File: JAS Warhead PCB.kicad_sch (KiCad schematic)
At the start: 8 parts, among them J7 Conn_01x02_Socket, U4 LD1117S50TR_SOT223

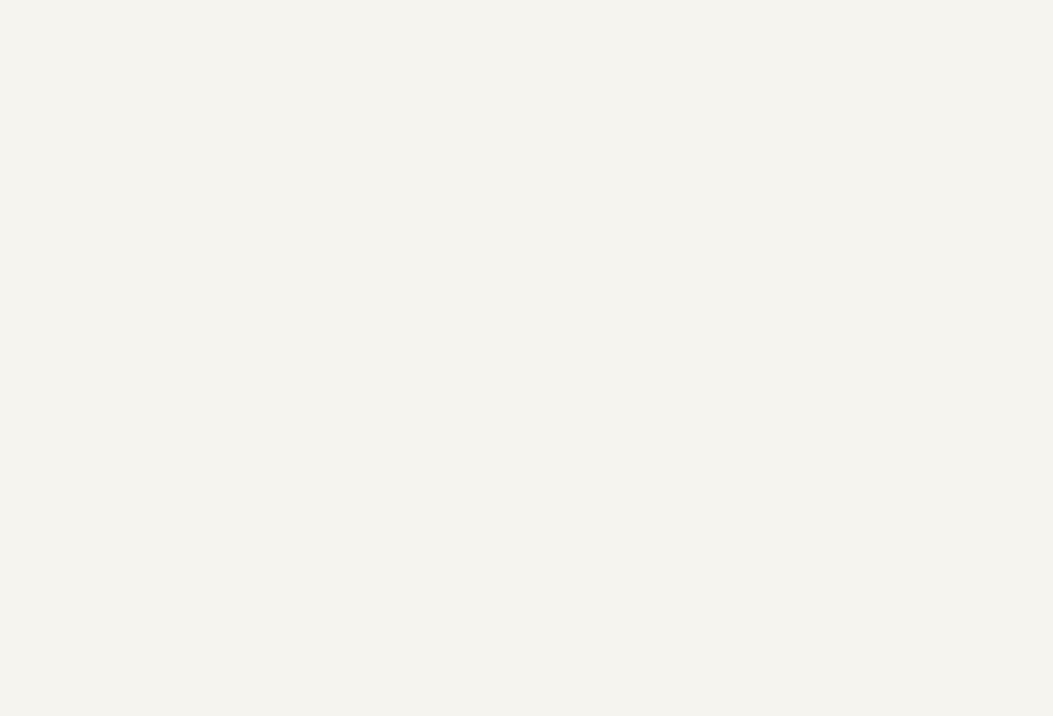
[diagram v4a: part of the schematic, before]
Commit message: adds relays
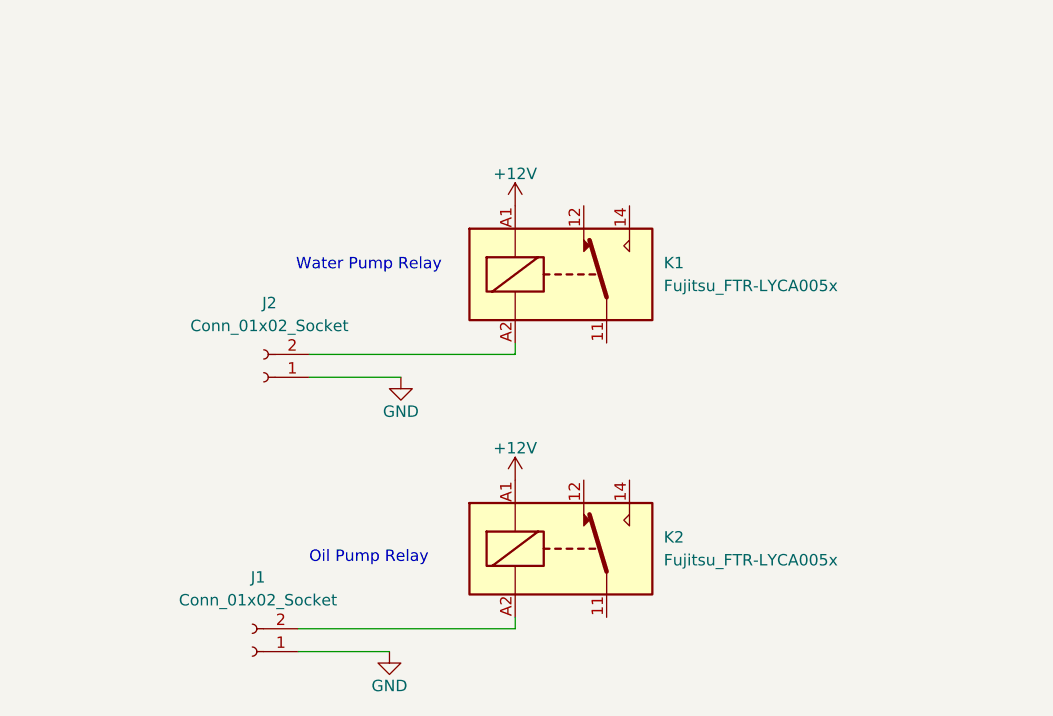
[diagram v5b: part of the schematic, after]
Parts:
- added J1, J2: Conn_01x02_Socket, TerminalBlock_4Ucon:TerminalBlock_4Ucon_1x02_P3.50mm_Vertical, symbol Connector:Conn_01x02_Socket
- added K1, K2: Fujitsu_FTR-LYCA005x, Relay_THT:Relay_SPDT_Fujitsu_FTR-LYCA005x_FormC_Vertical, symbol Relay:Fujitsu_FTR-LYCA005x
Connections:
- net +12V: now also K1.A1, K2.A1
- net GND: now also J1.1 (Pin_1), J2.1 (Pin_1)
- new net: J2.2 (Pin_2), K1.A2
- new net: J1.2 (Pin_2), K2.A2
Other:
- note added: "Oil Pump Relay"
- note added: "Water Pump Relay"

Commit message: relays
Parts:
- removed K1, K2: Fujitsu_FTR-LYCA005x, Relay_THT:Relay_SPDT_Fujitsu_FTR-LYCA005x_FormC_Vertical, symbol Relay:Fujitsu_FTR-LYCA005x
- added D1, D10: 1N4001, Diode_THT:D_DO-41_SOD81_P10.16mm_Horizontal, symbol Diode:1N4001
- added K1, K2: Panasonic_ALFG1PF12, Relay_THT:Relay_SPDT_Omron_G2RL-1-E, symbol Relay:Panasonic_ALFG1PF12
- added Q1, Q2: PN2222A, Package_TO_SOT_THT:TO-92_Inline, symbol Transistor_BJT:PN2222A
- added R1, R12: 4.7K, Resistor_SMD:R_0815_2038Metric, symbol Device:R
- added R10, R11: 50K, Resistor_SMD:R_2816_7142Metric_Pad3.20x4.45mm_HandSolder, symbol Device:R
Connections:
- net +12V: now also K1.14, K2.14, Q1.3 (C), Q2.3 (C)
- net GND: now also R10.2, R11.2
- net at J2.2 (Pin_2): now also K1.11
- net at J1.2 (Pin_2): now also K2.11
- new net: D10.1 (K), K2.A1
- new net: D10.2 (A), Q1.1 (E)
- new net: K2.A2, R11.1
- new net: Q1.2 (B), R12.1
- new net: Q2.2 (B), R1.1
- new net: D1.1 (K), K1.A1
- new net: K1.A2, R10.1
- new net: D1.2 (A), Q2.1 (E)
- new net RELAY1: R1.2
- new net RELAY2: R12.2
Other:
- moved on the sheet: J2

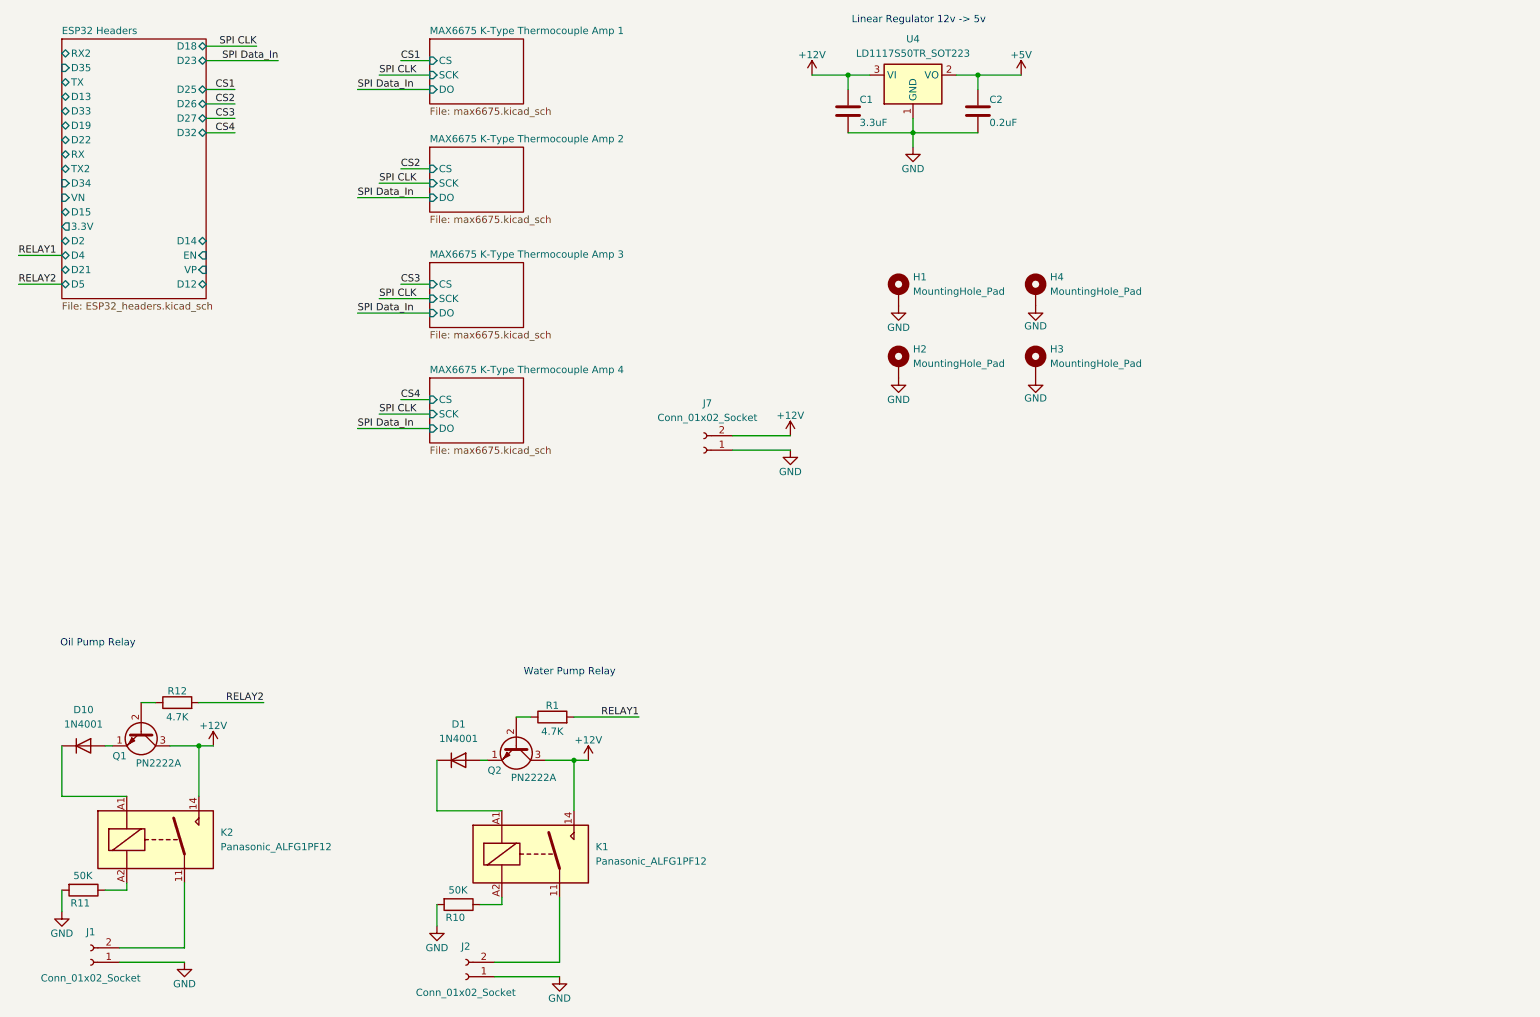
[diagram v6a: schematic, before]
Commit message: adds thermister locations
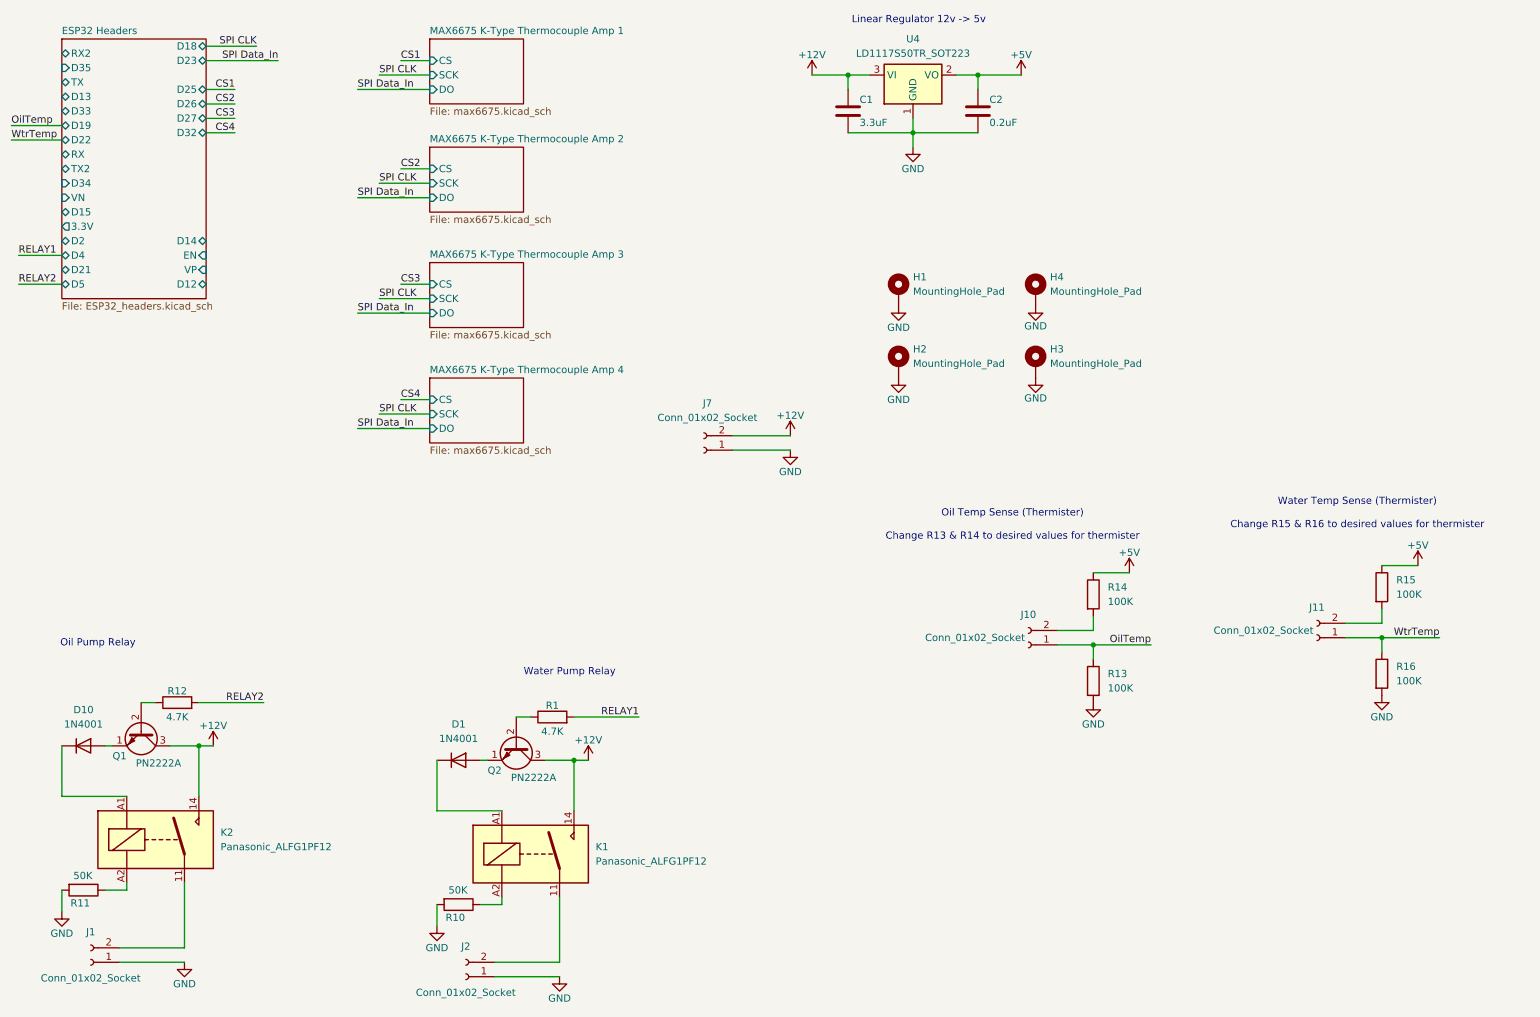
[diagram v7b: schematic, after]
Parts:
- added J10, J11: Conn_01x02_Socket, TerminalBlock_4Ucon:TerminalBlock_4Ucon_1x02_P3.50mm_Vertical, symbol Connector:Conn_01x02_Socket
- added R13, R14, R15, R16: 100K, Resistor_SMD:R_0603_1608Metric, symbol Device:R
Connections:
- net +5V: now also R14.1, R15.1
- net GND: now also R13.2, R16.2
- new net: J11.2 (Pin_2), R15.2
- new net: J10.2 (Pin_2), R14.2
- new net OilTemp: J10.1 (Pin_1), R13.1
- new net WtrTemp: J11.1 (Pin_1), R16.1
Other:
- note added: "Oil Temp Sense (Thermister) Change R13 & R14 to desired values for thermister"
- note added: "Water Temp Sense (Thermister) Change R15 & R16 to desired values for thermister"
- company: (none) -> Jet & Aeronatucs Society
- title: (none) -> Blast Shield

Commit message: new bom
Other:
- note added: "Main PWR"
- moved on the sheet: H1, H2, H3, H4, J10, J11, J7, R13, R14, R15, R16
